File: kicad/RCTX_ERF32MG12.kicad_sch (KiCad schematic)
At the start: 101 parts

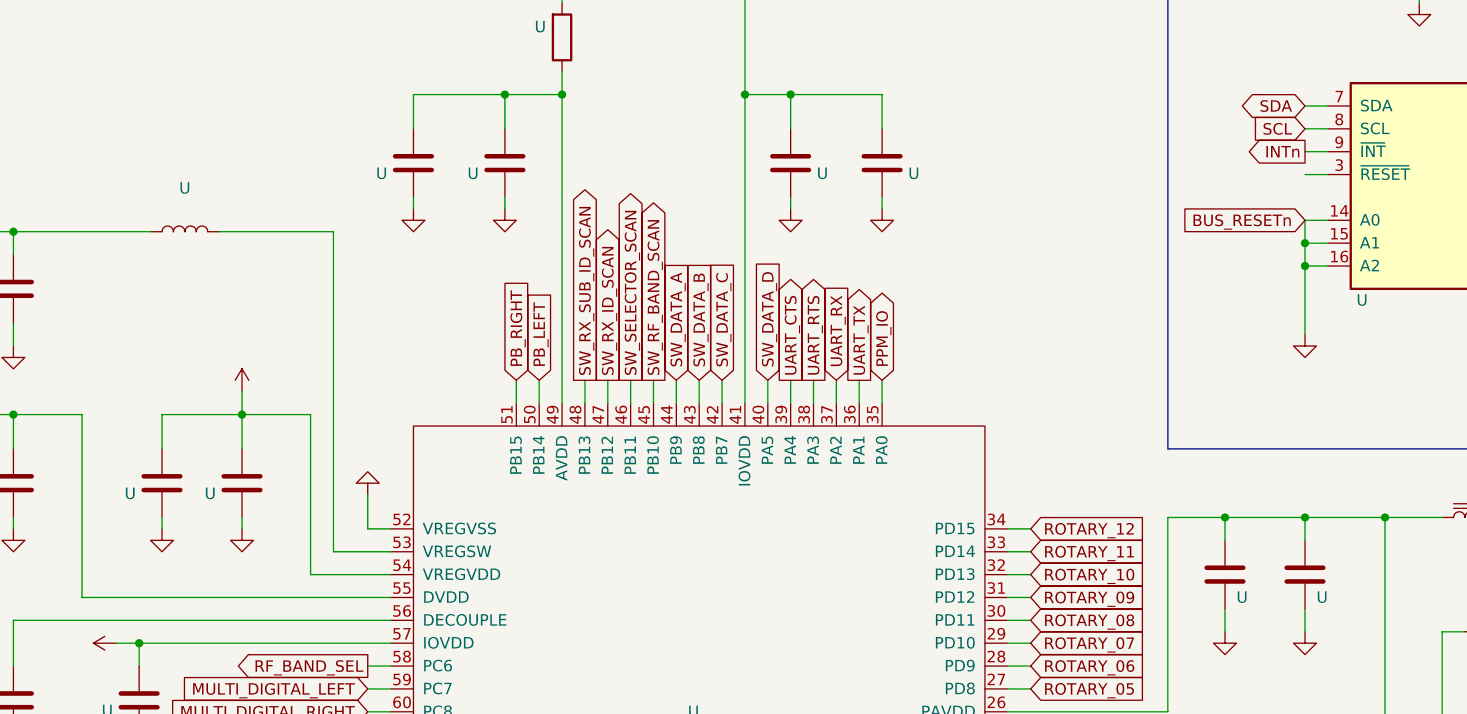
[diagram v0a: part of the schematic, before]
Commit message: Adding PIB USB BRIDGE UML state diagrams
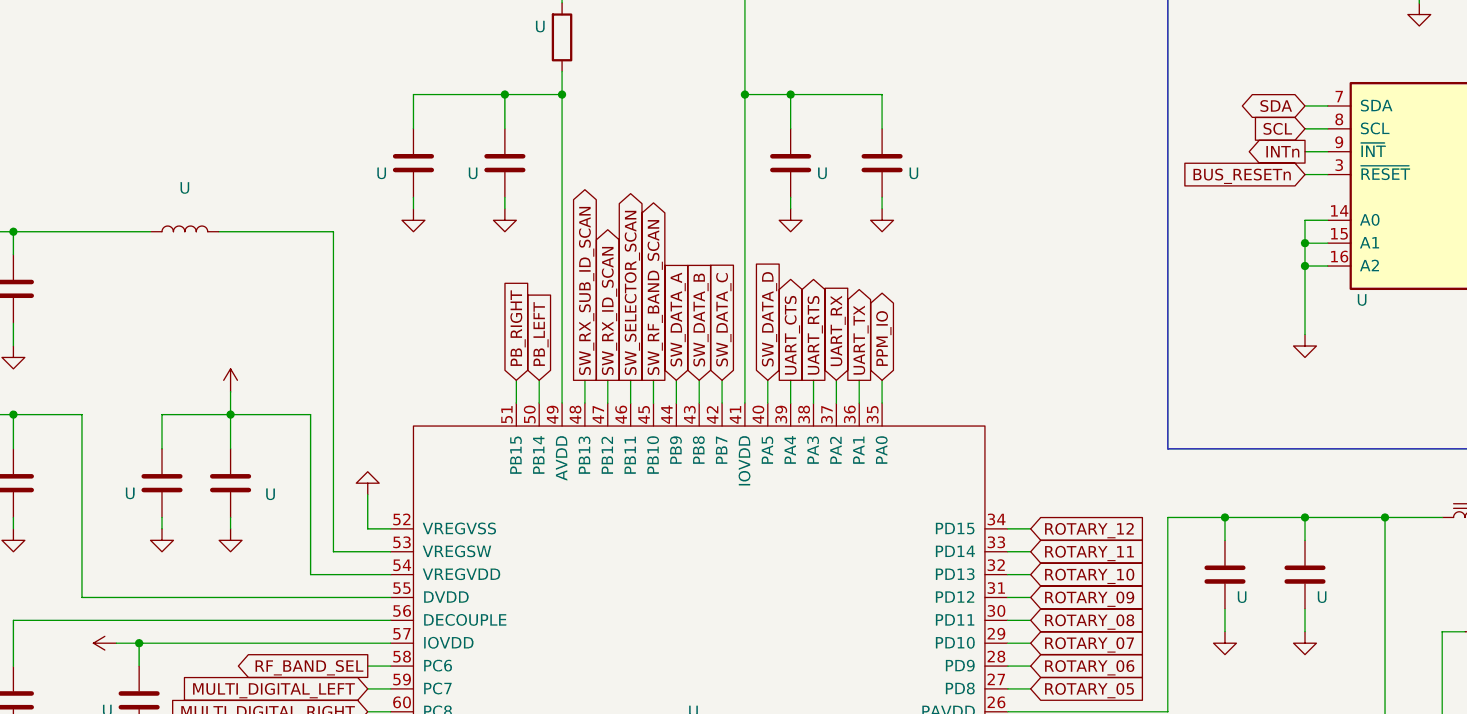
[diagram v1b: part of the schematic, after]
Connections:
- net GND: no longer U.11 (RC2), U.5 (PF3)
- net BUS_RESETn: now reaches U.3 (~{RESET})
- net BUS_RESETn: now also U.11 (RC2), U.5 (PF3)
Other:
- moved on the sheet: U

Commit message: Adding PIB USB BRIDGE UML state diagrams - WIP
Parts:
- removed U: (no value), symbol PIC_USB_BRIDGE:PIC16(L)F1459-I_ML
- removed U: (no value), symbol conn:USB_OTG
- removed U (x4): (no value), symbol device:C
- removed U: (no value), symbol nxp_sc18is602b:SC18IS602B
- removed U: (no value), symbol conn:Conn_02x06_Odd_Even
- removed U: (no value), symbol device:Q_PMOS_DGS
- removed U: (no value), symbol device:D_Schottky
- removed U (x2): (no value), symbol device:R
- removed U: (no value), symbol RCTX-rescue:SW_Push-switches
- added C1, C2: 33p, symbol device:C
- added D1: D_Schottky, symbol device:D_Schottky
- added J21: BUZZER, symbol Connector_Generic:Conn_01x02
- added J22: USB_OTG, symbol conn:USB_OTG
- added P1: Nokia 5110 display, symbol conn:Conn_02x06_Odd_Even
- added Q1: Q_PMOS_DGS, symbol device:Q_PMOS_DGS
- added R1: 100k, symbol device:R
- added SW1: RESET, symbol RCTX-rescue:SW_Push-switches
- added U1: PIC16(L)F1459-I_ML, symbol PIC_USB_BRIDGE:PIC16(L)F1459-I_ML
- C? (x3): renamed from U; value (none) -> 13p
- C?: renamed from U; value (none) -> 3p
- C? (x2): renamed from U; value (none) -> 10p
- C?, L?: renamed from U; value (none) -> 220n
- C? (x8): renamed from U; value (none) -> 100n
- C? (x3), L?: renamed from U; value (none) -> 4u7
- C? (x8): renamed from U; value (none) -> 1u
- C? (x2): renamed from U; value (none) -> 10u
- C?: renamed from U; value (none) -> 10n
- C?: renamed from U; value (none) -> 10u 16V
- C? (x2): renamed from U; value (none) -> 1n
- C? (x6): renamed from U; value (none) -> 100p
- D? (x4): renamed from U; value (none) -> 1N4148; footprint (none) -> Diodes_THT:D_5W_P5.08mm_Vertical_KathodeUp
- HEX_SW?: renamed from U; value (none) -> RF_BAND_SEL; footprint (none) -> Buttons_Switches_THT:Nidec_Copal_SH-7010C
- J?: renamed from U; value (none) -> SWITCHES
- J?: renamed from U; value (none) -> 50 Ohm 433-460 MHz Antenna
- J?: renamed from U; value (none) -> 50 Ohm 2.4 GHz Antenna
- J?: renamed from U; value (none) -> 50 Ohm 13-79 MHz Antenna
- L?: renamed from U; value (none) -> CBF102WB
- L? (x2): renamed from U; value (none) -> 390n
- L? (x2): renamed from U; value (none) -> 470n
- L? (x2): renamed from U; value (none) -> BLM18AG601SN1
- L? (x2): renamed from U; value (none) -> L
- L?: renamed from U; value (none) -> 36n
- P?: renamed from U; value (none) -> POWER_IN; footprint (none) -> Connectors_Samtec:SL-104-X-XX_1x04
- P? (x2): renamed from U; value (none) -> KEYPAD
- P?: renamed from U; value (none) -> SW
- P?: renamed from U; value (none) -> BUZZ
- P?: renamed from U; value (none) -> POWER
- P?: renamed from U; value (none) -> SD Card
- P?: renamed from U; value (none) -> Left SW LEDs
- P?: renamed from U; value (none) -> Right SW LEDs
- P?: renamed from U; value (none) -> MULTI_PROP_1
- P?: renamed from U; value (none) -> MULTI_PROP_2
- P?: renamed from U; value (none) -> AUX_DB15_PORT
- R?: renamed from U; value (none) -> 10
- R?: renamed from U; value (none) -> 1R
- RV?: renamed from U; value (none) -> POT; footprint (none) -> Potentiometers:Potentiometer_Trimmer_ACP_CA6v_Horizontal
- U?: renamed from U; value (none) -> KTD2061
- U?: renamed from U; value (none) -> EFR32MG12P433F1024GM68; footprint (none) -> Footprint
- U?: renamed from U; value (none) -> RLP-83+
- U?: renamed from U; value (none) -> RBP-440+
- U?: renamed from U; value (none) -> LM1117-3.3
- U?: renamed from U; value (none) -> LM1117-5.0
- U? (x2): renamed from U; value (none) -> MAX2650; footprint (none) -> smd-semi:SOT-143
- U?: renamed from U; value (none) -> ADE-1+; footprint (none) -> RF_Mini-Circuits:Mini-Circuits_CD542_LandPatternPL-052
- U? (x2): renamed from U; value (none) -> TLV70245_SOT23-5; footprint (none) -> TO_SOT_Packages_SMD:SOT-23-5
- Y?: renamed from U; value (none) -> 38.400 MHz
- Y?: renamed from U; value (none) -> 514CCAXXXXXXCAG; footprint (none) -> Si500D
- ZD?: renamed from U; value (none) -> ZENER; footprint (none) -> Diodes_THT:D_5W_P5.08mm_Vertical_KathodeUp
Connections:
- net +3V3: now also P1.1 (Pin_1)
- net +5V: now also Q1.1 (D)
- net BUZZER: now also J21.1 (Pin_1), U1.20 (RA4)
- net GND: now also C1.1, C2.2, J21.2 (Pin_2), J22.6 (Shield), P1.10 (Pin_10), P1.12 (Pin_12), P1.2 (Pin_2), P1.4 (Pin_4), P1.6 (Pin_6), P1.8 (Pin_8), R1.2, SW1.2, U1.17 (VSS)
- net SOC_RESETn: now also U1.5 (RC6)
- net SWCLK: now also U1.2 (RC5)
- net SWDIO: now also U1.3 (RC4)
- net SWO: now also U1.4 (RC3)
- net USB_RX: now also U1.9 (RX)
- net USB_TX: now also U1.7 (TX)
- net /SD_CE: now reaches P?.9 (Pin_9)
- net /SD_CE: now also U1.11 (RC2)
- net SCK: now reaches P?.7 (Pin_7)
- net SCK: now also P1.7 (Pin_7), U1.8 (SCK)
- net SDO: now reaches P?.3 (Pin_3)
- net SDO: now also P1.5 (Pin_5), U1.6 (SDO)
- net SDI: now reaches P?.5 (Pin_5)
- net SDI: now also U1.10 (SDI)
- net BUS_RESETn: no longer names the net of U?.5 (PF3)
- net INTn: no longer names the net of U?.13 (PF7)
- new net: D1.2 (A), J22.5 (GND), Q1.2 (G), R1.1
- new net: C2.1, D1.1 (K), Q1.3 (S), U1.18 (VDD)
- new net: J22.1 (VBUS), SW1.1, U1.1 (Vpp)
- new net: J22.2 (D-), U1.15 (D-)
- new net: J22.3 (D+), U1.16 (D+)
- new net: C1.2, U1.14 (Vusb3v3)
- new net LCD_D/C: P1.9 (Pin_9), U1.13 (RC0)
- new net /LCD_CE: P1.3 (Pin_3), U1.12 (RC1)
- new net /LCD_RESET: P1.11 (Pin_11), U1.19 (RA5)
- no-connect marks 4 -> 3
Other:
- note added: "- UART bridge for SD card and Nokia 5110 LCD - USB Adapter for: CMSIS-DAP / COM port / Mass storage (SD Card)"
- note removed: "I2C to SPI bridge for SD Card and Nokia 5110 display"
- note removed: "USB bridge to programming (SWD/ICSP), communication (UART) and SD card (I2C)"
- moved on the sheet: C?, D?, HEX_SW?, J?, L?, P?, R?, RV?, U?, Y?, ZD?

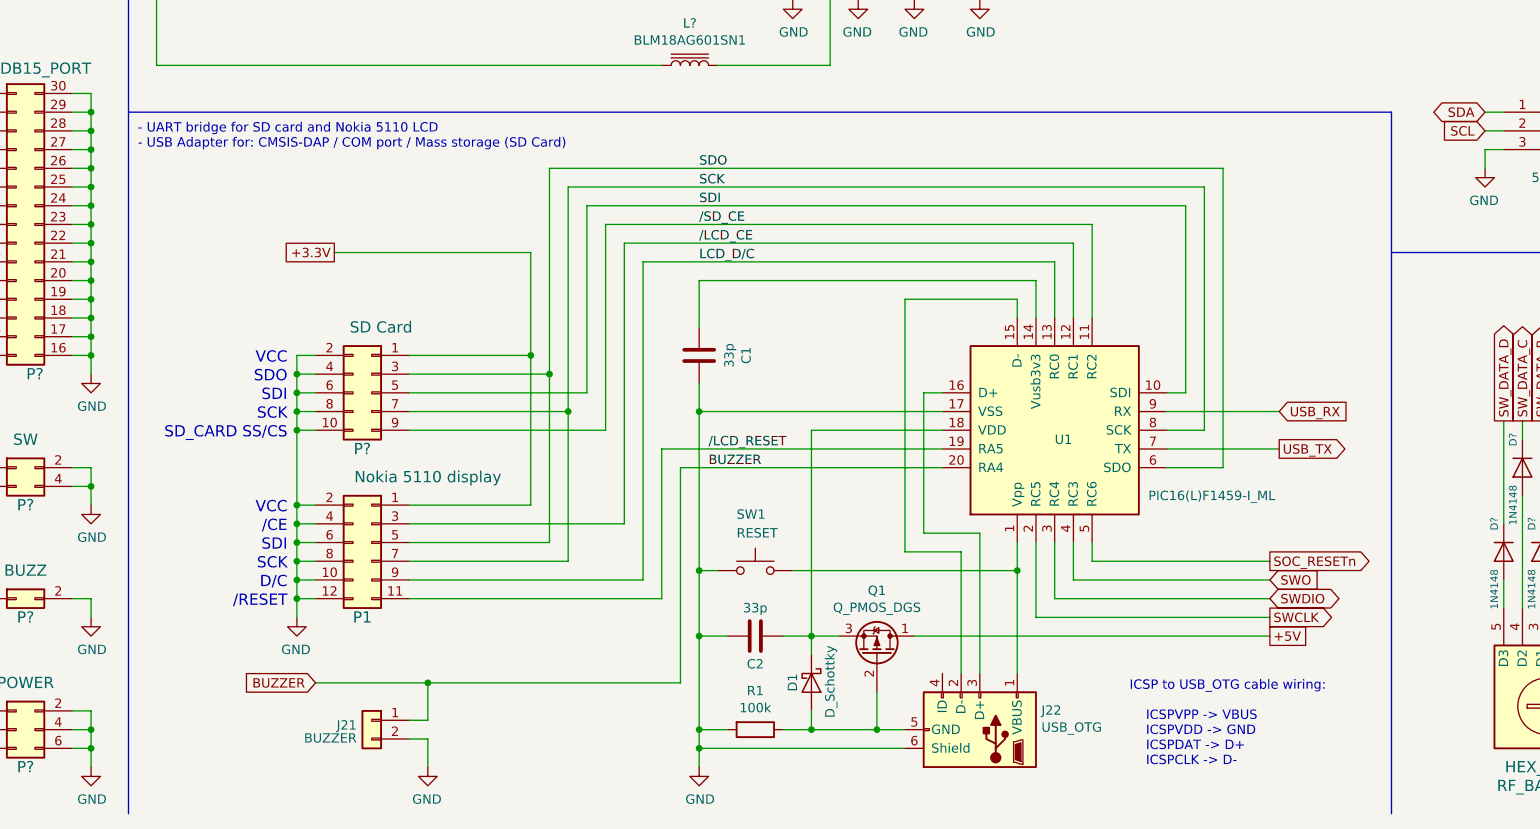
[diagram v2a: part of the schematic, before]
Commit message: Reset PIC by cutting off Vdd via a n/c SW instead of grounding the USB VBUS on Vpp via a n/o SW
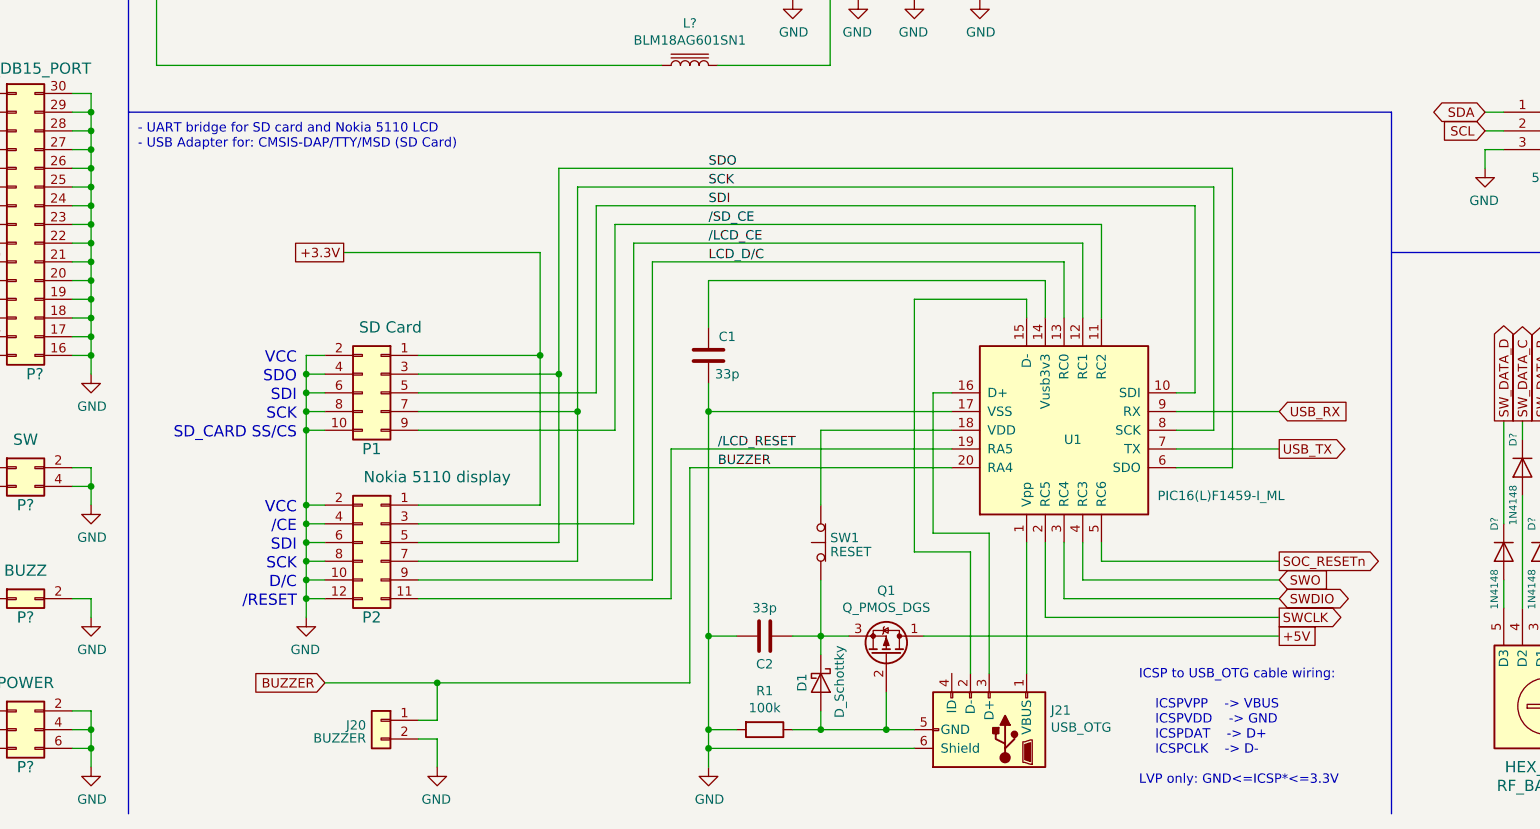
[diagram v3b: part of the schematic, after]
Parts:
- removed J21: BUZZER, symbol Connector_Generic:Conn_01x02
- removed J22: USB_OTG, symbol conn:USB_OTG
- removed P1: Nokia 5110 display, symbol conn:Conn_02x06_Odd_Even
- removed P?: SD Card, symbol conn:Conn_02x05_Odd_Even
- removed SW1: RESET, symbol RCTX-rescue:SW_Push-switches
- added J20: BUZZER, symbol Connector_Generic:Conn_01x02
- added J21: USB_OTG, symbol conn:USB_OTG
- added P1: SD Card, symbol conn:Conn_02x05_Odd_Even
- added P2: Nokia 5110 display, symbol conn:Conn_02x06_Odd_Even
- added SW1: RESET, symbol switches:SW_Push_Open
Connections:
- net +3V3: now also P1.1 (Pin_1), P2.1 (Pin_1)
- net BUZZER: now also J20.1 (Pin_1)
- net GND: now also J20.2 (Pin_2), J21.6 (Shield), P1.10 (Pin_10), P1.2 (Pin_2), P1.4 (Pin_4), P1.6 (Pin_6), P1.8 (Pin_8), P2.10 (Pin_10), P2.12 (Pin_12), P2.2 (Pin_2), P2.4 (Pin_4), P2.6 (Pin_6), P2.8 (Pin_8)
- net LCD_D/C: now also P2.9 (Pin_9)
- net SCK: now also P1.7 (Pin_7), P2.7 (Pin_7)
- net SDI: now also P1.5 (Pin_5)
- net SDO: now also P1.3 (Pin_3), P2.5 (Pin_5)
- net /LCD_CE: now also P2.3 (Pin_3)
- net /LCD_RESET: now also P2.11 (Pin_11)
- net /SD_CE: now also P1.9 (Pin_9)
- net at D1.2 (A), Q1.2 (G), R1.1: now also J21.5 (GND)
- net at C2.1, D1.1 (K), Q1.3 (S): now also SW1.1 (A); no longer U1.18 (VDD)
- net at U1.1 (Vpp): now also J21.1 (VBUS)
- net at U1.15 (D-): now also J21.2 (D-)
- net at U1.16 (D+): now also J21.3 (D+)
- new net: SW1.2 (B), U1.18 (VDD)
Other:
- note added: "- UART bridge for SD card and Nokia 5110 LCD - USB Adapter for: CMSIS-DAP/TTY/MSD (SD Card)"
- note added: "ICSP to USB_OTG cable wiring: ICSPVPP -> VBUS ICSPVDD -> GND ICSPDAT -> D+ ICSPCLK -> D- LVP only: GND<=ICSP*<=3.3V"
- note removed: "- UART bridge for SD card and Nokia 5110 LCD - USB Adapter for: CMSIS-DAP / COM port / Mass storage (SD Card)"
- note removed: "ICSP to USB_OTG cable wiring: ICSPVPP -> VBUS ICSPVDD -> GND ICSPDAT -> D+ ICSPCLK -> D-"
